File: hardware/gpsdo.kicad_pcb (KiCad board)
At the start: 2 copper layers, 63.5 x 63.5 mm, 82 parts, among them J1 Conn_Coaxial, J2 Conn_Coaxial, J3 Conn_Coaxial, J4 Conn_Coaxial, J5 Conn_01x08, J6 Conn_01x02, J7 Conn_01x02, Q1 MMBT3906LT1G, Q2 MMBT3906LT1G, U1 74LVC1G14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

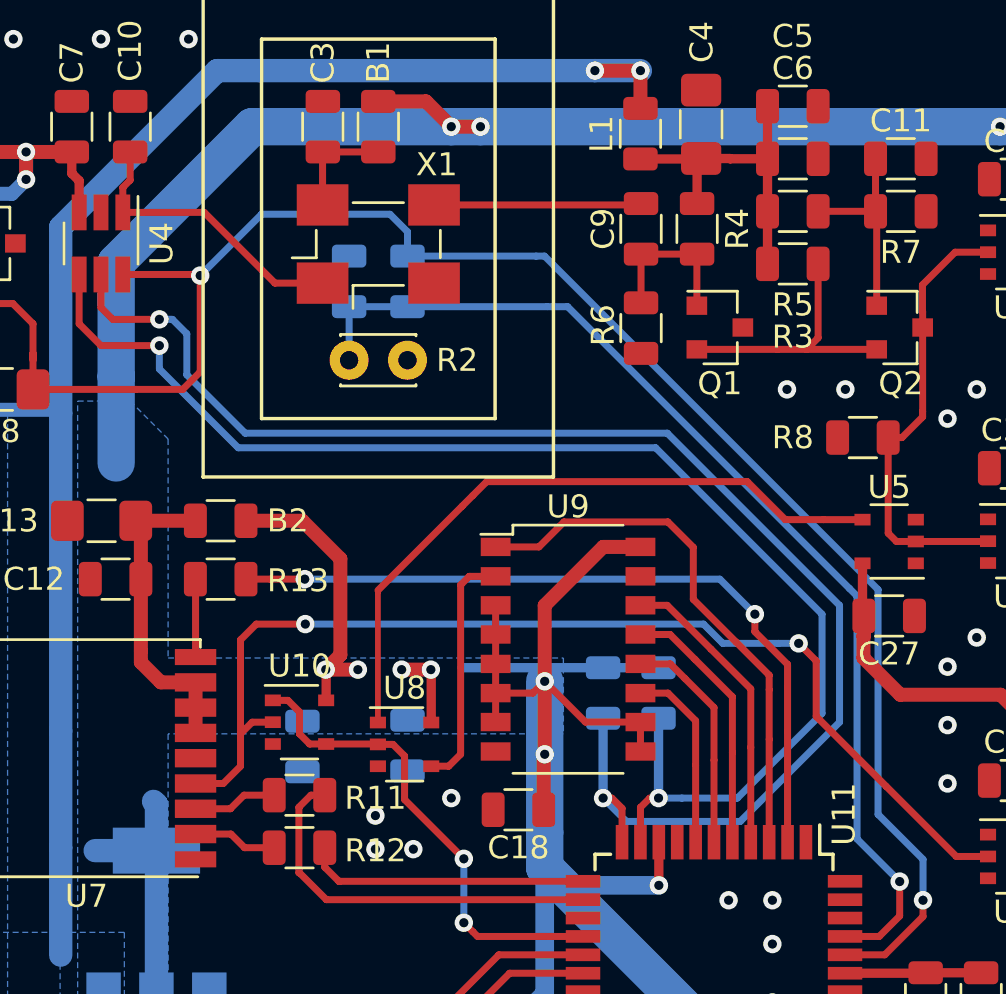
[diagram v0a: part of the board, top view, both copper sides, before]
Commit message: symbol update
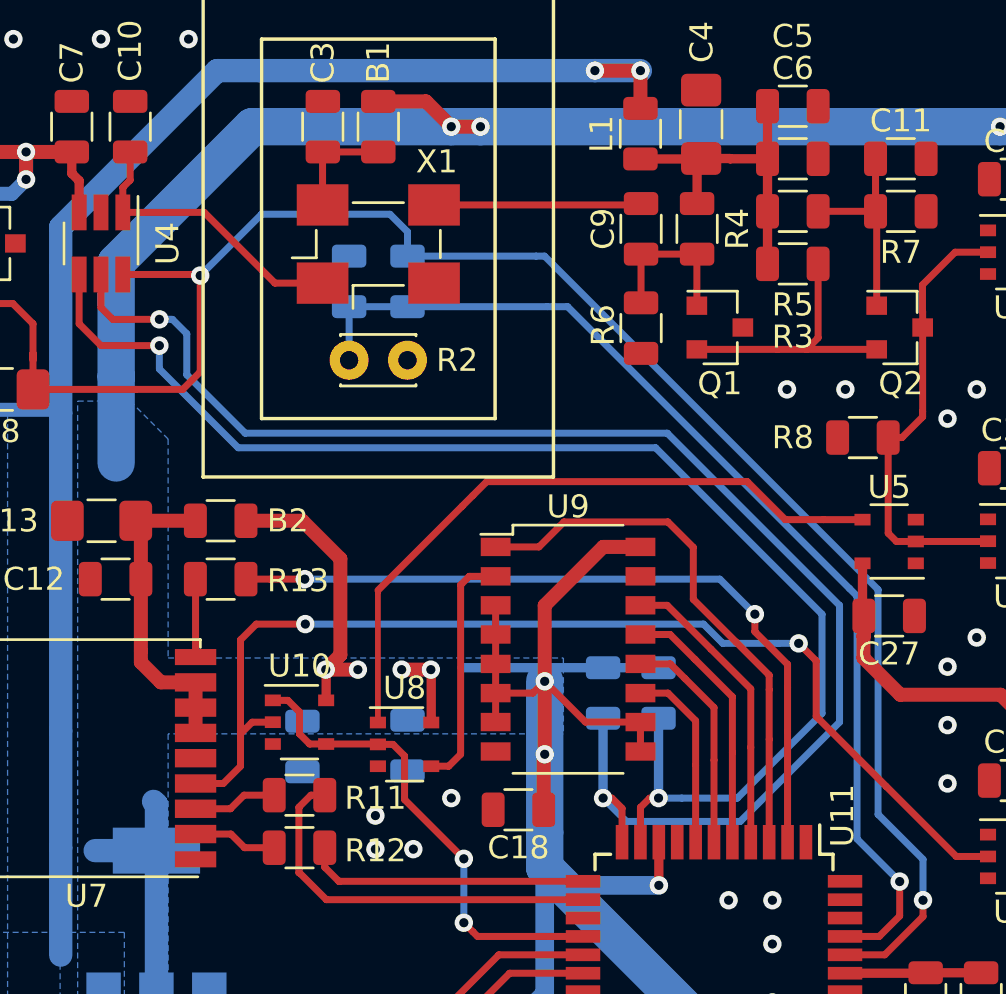
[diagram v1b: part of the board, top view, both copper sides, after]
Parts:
- U4: value MCP4726 -> MCP4726AxT-E-CH
- X1: footprint obbo_footprints:Oscillator_SMD_ILSI-4Pin_5.0mmx3.2mm_HandSoldering -> obbo_footprints:Oscillator_SMD_ILSI-4Pin_5.0mm_3.2mm_HandSoldering
